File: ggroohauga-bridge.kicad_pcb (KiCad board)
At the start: 2 copper layers, 98.5 x 31 mm, 12 parts

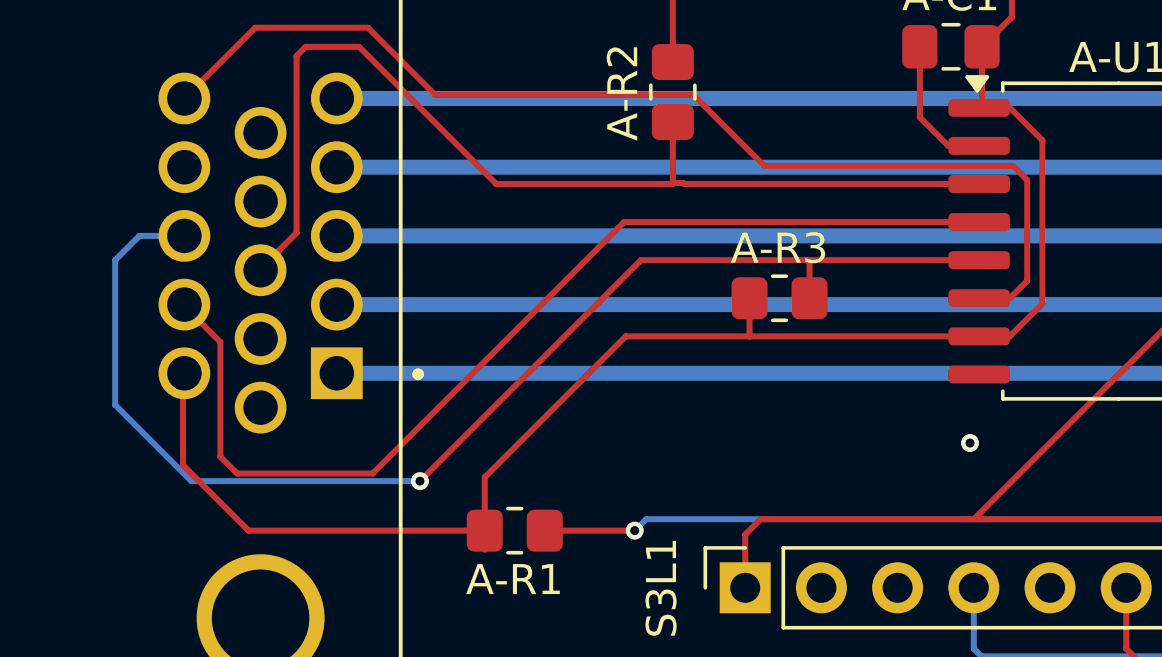
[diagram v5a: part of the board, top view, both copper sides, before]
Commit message: Move pull-up from AMP_RX to AMP_TX
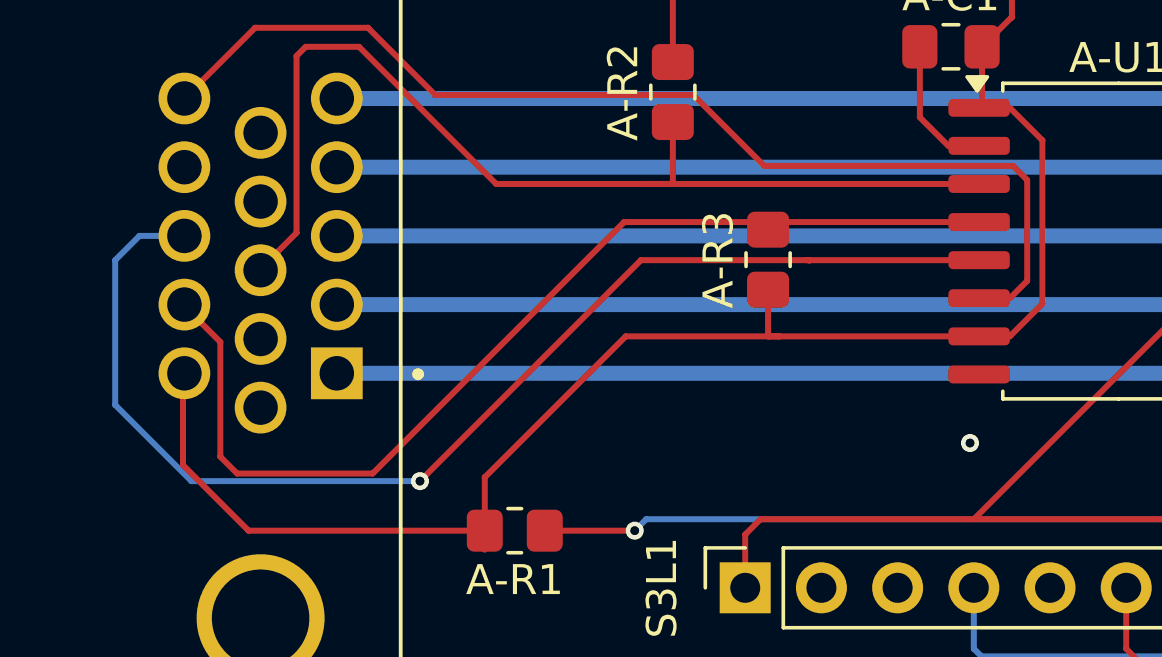
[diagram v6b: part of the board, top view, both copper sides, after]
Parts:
- moved A-R3 1.34 mm to (82.3, 66.5), turned to 90 degrees
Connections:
- A-R3 pad 2: /Common/AMP_RX -> /Common/AMP_TX
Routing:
- net /Common/AMP_RX: track 41.7 -> 40.5 mm
- net /Common/AMP_DETECT: track 34.5 -> 35.5 mm
- net /Common/AMP_TX: track 34.6 -> 33.8 mm
- net /Common/AMP_POWER_IN: track 74.8 -> 75.5 mm
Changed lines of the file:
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@@
 	(footprint "Resistor_SMD:R_0805_2012Metric_Pad1.20x1.40mm_HandSolder"
 		(layer "F.Cu")
-		(at 82.677 67.818)
+		(at 82.296 66.532 90)
 		(descr "Resistor SMD 0805 (2012 Metric), square (rectangular) end terminal, IPC-7351 nominal with elongated pad for handsoldering. (Body size source: IPC-SM-782 page 72, https://www.pcb-3d.com/wordpress/wp-content/uploads/ipc-sm-782a_amendment_1_and_2.pdf), generated with kicad-footprint-generator")
 		(tags "resistor handsolder")
 		(property "Reference" "A-R3"
-			(at 0 -1.65 0)
+			(at 0 -1.65 90)
 			(layer "F.SilkS")
 			(effects
@@
 		)
 		(property "Value" "10kΩ"
-			(at 0 1.65 0)
+			(at 0 1.65 90)
 			(layer "F.Fab")
 			(effects
@@
 		)
 		(property "Datasheet" ""
-			(at 0 0 0)
+			(at 0 0 90)
 			(layer "F.Fab")
 			(hide yes)
@@
 		)
 		(property "Description" "Resistor"
-			(at 0 0 0)
+			(at 0 0 90)
 			(layer "F.Fab")
 			(hide yes)
@@
 		)
 		(fp_line
-			(start -1.85 -0.95)
-			(end 1.85 -0.95)
+			(start 1.85 -0.95)
+			(end 1.85 0.95)
 			(stroke
 				(width 0.05)
@@
 		)
 		(fp_line
-			(start -1.85 0.95)
-			(end -1.85 -0.95)
+			(start -1.85 -0.95)
+			(end 1.85 -0.95)
 			(stroke
 				(width 0.05)
@@
 		)
 		(fp_line
-			(start 1.85 -0.95)
-			(end 1.85 0.95)
+			(start 1.85 0.95)
+			(end -1.85 0.95)
 			(stroke
 				(width 0.05)
@@
 		)
 		(fp_line
-			(start 1.85 0.95)
-			(end -1.85 0.95)
+			(start -1.85 0.95)
+			(end -1.85 -0.95)
 			(stroke
 				(width 0.05)
@@
 		)
 		(fp_line
-			(start -1 -0.625)
-			(end 1 -0.625)
+			(start 1 -0.625)
+			(end 1 0.625)
 			(stroke
 				(width 0.1)
@@
 		)
 		(fp_line
-			(start -1 0.625)
-			(end -1 -0.625)
+			(start -1 -0.625)
+			(end 1 -0.625)
 			(stroke
 				(width 0.1)
@@
 		)
 		(fp_line
-			(start 1 -0.625)
-			(end 1 0.625)
+			(start 1 0.625)
+			(end -1 0.625)
 			(stroke
 				(width 0.1)
@@
 		)
 		(fp_line
-			(start 1 0.625)
-			(end -1 0.625)
+			(start -1 0.625)
+			(end -1 -0.625)
 			(stroke
 				(width 0.1)
@@
 		)
 		(fp_text user "${REFERENCE}"
-			(at 0 0 0)
+			(at 0 0 90)
 			(layer "F.Fab")
 			(effects
@@
 		)
 		(pad "1" smd roundrect
-			(at -1 0)
+			(at -1 0 90)
 			(size 1.2 1.4)
 			(layers "F.Cu" "F.Mask" "F.Paste")
@@
 		)
 		(pad "2" smd roundrect
-			(at 1 0)
+			(at 1 0 90)
 			(size 1.2 1.4)
 			(layers "F.Cu" "F.Mask" "F.Paste")
 			(roundrect_rratio 0.208333)
-			(net 5 "/Common/AMP_RX")
+			(net 4 "/Common/AMP_TX")
 			(pintype "passive")
 		)
@@
 	)
 	(segment
-		(start 81.677 69.072)
-		(end 81.693 69.088)
+		(start 82.296 67.532)
+		(end 82.296 69.088)
 		(width 0.2)
 		(layer "F.Cu")
@@
 	)
 	(segment
-		(start 81.693 69.088)
+		(start 82.296 69.088)
+		(end 82.677 69.088)
+		(width 0.2)
+		(layer "F.Cu")
+		(net 3)
+	)
+	(segment
+		(start 72.8516 76.2)
+		(end 72.8516 73.787)
+		(width 0.2)
+		(layer "F.Cu")
+		(net 3)
+	)
+	(segment
+		(start 82.677 69.088)
 		(end 89.33 69.088)
 		(width 0.2)
@@
 	)
 	(segment
-		(start 89.4295 59.436)
-		(end 89.4295 61.3685)
+		(start 77.5506 69.088)
+		(end 82.677 69.088)
 		(width 0.2)
 		(layer "F.Cu")
@@
 	)
 	(segment
-		(start 81.677 67.818)
-		(end 81.677 69.072)
+		(start 89.4295 59.436)
+		(end 89.4295 61.3685)
 		(width 0.2)
 		(layer "F.Cu")
@@
 	)
 	(segment
-		(start 81.677 69.072)
-		(end 81.661 69.088)
-		(width 0.2)
-		(layer "F.Cu")
-		(net 3)
-	)
-	(segment
 		(start 72.8516 75.565)
 		(end 64.9776 75.565)
@@
 	)
 	(segment
-		(start 72.8516 76.2)
-		(end 72.8516 73.787)
-		(width 0.2)
-		(layer "F.Cu")
-		(net 3)
-	)
-	(segment
 		(start 90.424 53.34)
 		(end 90.424 58.4575)
@@
 	)
 	(segment
-		(start 72.8516 73.787)
-		(end 77.5506 69.088)
-		(width 0.2)
-		(layer "F.Cu")
-		(net 3)
-	)
-	(segment
 		(start 90.424 58.4575)
 		(end 90.408 58.4575)
@@
 	)
 	(segment
-		(start 77.5506 69.088)
-		(end 81.661 69.088)
+		(start 72.8516 73.787)
+		(end 77.5506 69.088)
 		(width 0.2)
 		(layer "F.Cu")
@@
 	)
 	(segment
-		(start 69.115618 73.66)
+		(start 82.042 65.278)
 		(end 77.497618 65.278)
 		(width 0.2)
@@
 	(segment
 		(start 64.0378 69.2742)
-		(end 64.0378 73.1012)
+		(end 62.7928 68.0292)
 		(width 0.2)
 		(layer "F.Cu")
@@
 	(segment
 		(start 64.0378 73.1012)
-		(end 64.5966 73.66)
+		(end 64.0378 69.2742)
 		(width 0.2)
 		(layer "F.Cu")
@@
 	)
 	(segment
-		(start 62.7928 68.0292)
-		(end 64.0378 69.2742)
+		(start 64.5966 73.66)
+		(end 64.0378 73.1012)
 		(width 0.2)
 		(layer "F.Cu")
@@
 	(segment
 		(start 77.497618 65.278)
+		(end 69.115618 73.66)
+		(width 0.2)
+		(layer "F.Cu")
+		(net 4)
+	)
+	(segment
+		(start 82.804 65.278)
 		(end 89.33 65.278)
 		(width 0.2)
@@
 	)
 	(segment
-		(start 64.5966 73.66)
-		(end 69.115618 73.66)
+		(start 69.115618 73.66)
+		(end 64.5966 73.66)
 		(width 0.2)
 		(layer "F.Cu")
@@
 	)
 	(segment
-		(start 83.677 67.818)
-		(end 83.677 66.564)
-		(width 0.2)
-		(layer "F.Cu")
-		(net 5)
-	)
-	(segment
 		(start 83.566 66.548)
 		(end 83.693 66.548)
@@
 	)
 	(segment
-		(start 79.47 63.976)
-		(end 79.502 64.008)
+		(start 78.105 64.008)
+		(end 73.2326 64.008)
 		(width 0.2)
 		(layer "F.Cu")
@@
 	)
 	(segment
-		(start 79.121 63.976)
-		(end 79.47 63.976)
+		(start 89.33 64.008)
+		(end 78.105 64.008)
 		(width 0.2)
 		(layer "F.Cu")
@@
 	(segment
 		(start 79.121 64.008)
-		(end 73.2326 64.008)
+		(end 78.105 64.008)
 		(width 0.2)
 		(layer "F.Cu")
@@
 		(width 0.2)
 		(layer "F.Cu")
-		(net 7)
-	)
-	(segment
-		(start 79.502 64.008)
-		(end 89.33 64.008)
-		(width 0.2)
-		(layer "F.Cu")

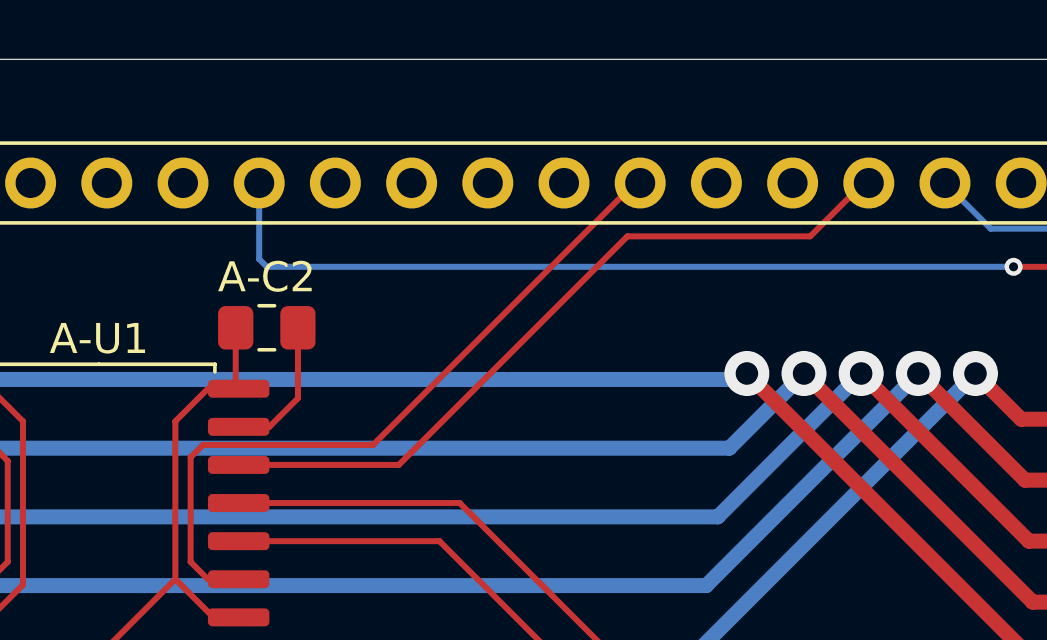
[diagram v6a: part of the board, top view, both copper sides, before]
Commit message: Fix GPIO assignments
Stop using GPIO 14 because the pull-up isn't working reliably on my LOLIN
S3 board even when floating and I don't have another one to test it with.

Don't use GPIO 35 on the DevKitC-1 board because that conflicts with the
Octal PSRAM.
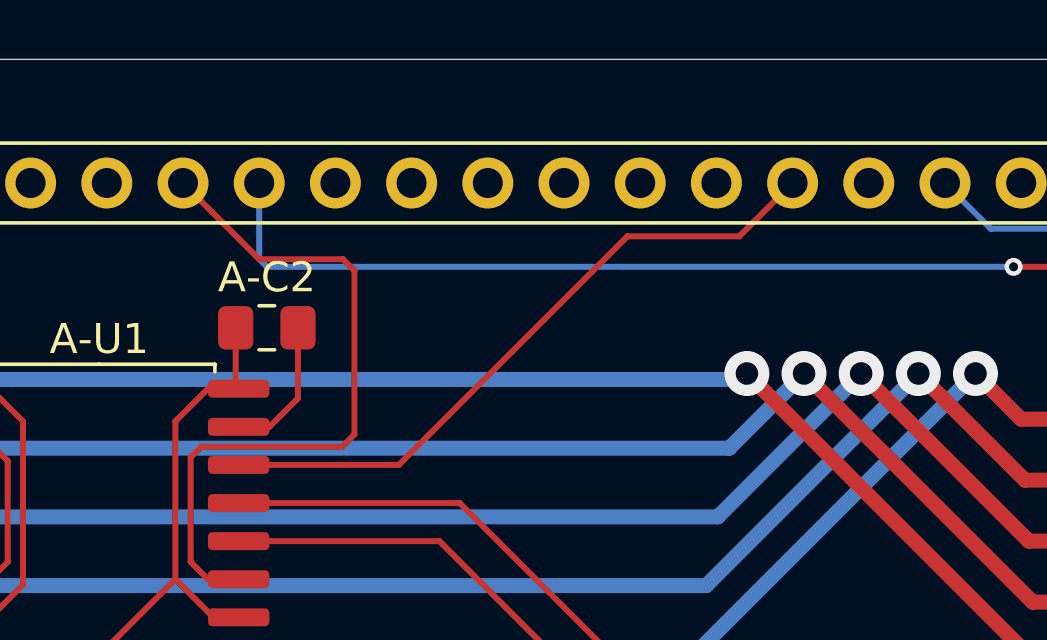
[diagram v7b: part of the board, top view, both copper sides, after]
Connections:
- A-U1 pad 11: /Common/GPIO_L48_C35_M36/CON_ANNOUNCE -> /Common/GPIO_L41_C41_M42/CON_ANNOUNCE
- A-U1 pad 14: /Common/GPIO_L14_C48_M33/AMP_DETECT -> /Common/GPIO_L21_C21_M21/AMP_DETECT
- S3R1 pad 13: /Common/GPIO_L48_C35_M36/CON_ANNOUNCE -> unconnected-(S3R1-Pin_13-Pad13)
- S3R1 pad 14: GND -> unconnected-(S3R1-Pin_14-Pad14)
- S3R1 pad 15: GND -> /Common/GPIO_L21_C21_M21/AMP_DETECT
- S3R1 pad 16: /Common/GPIO_L14_C48_M33/AMP_DETECT -> GND
- S3R1 pad 7: GND -> /Common/GPIO_L41_C41_M42/CON_ANNOUNCE
- S3R1 pad 9: GND -> unconnected-(S3R1-Pin_9-Pad9)
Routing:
- net /Common/GPIO_L14_C48_M33/AMP_DETECT: track 24.7 -> 0.00 mm
- net /Common/GPIO_L48_C35_M36/CON_ANNOUNCE: track 23.9 -> 0.00 mm
- net /Common/GPIO_L41_C41_M42/CON_ANNOUNCE: track 0.00 -> 23.5 mm
- net /Common/GPIO_L21_C21_M21/AMP_DETECT: track 0.00 -> 22.4 mm
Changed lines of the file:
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@@
 	(net 16 "/Common/GPIO_L9_C9_M13{slash}AMP_TX")
 	(net 17 "/Common/GPIO_L10_C10_M14{slash}AMP_RX")
-	(net 18 "/Common/GPIO_L48_C35_M36{slash}CON_ANNOUNCE")
-	(net 19 "/Common/GPIO_L14_C48_M33{slash}AMP_DETECT")
+	(net 18 "/Common/GPIO_L41_C41_M42{slash}CON_ANNOUNCE")
+	(net 19 "/Common/GPIO_L21_C21_M21{slash}AMP_DETECT")
 	(net 20 "+3.3V")
 	(net 21 "/Common/GPIO_L17_C17_M8{slash}CON_DETECT")
@@
 	(net 48 "unconnected-(C-J1-Pad7)")
 	(net 49 "unconnected-(S3L1-Pin_2-Pad2)")
+	(net 50 "unconnected-(S3R1-Pin_14-Pad14)")
+	(net 51 "unconnected-(S3R1-Pin_9-Pad9)")
+	(net 52 "unconnected-(S3R1-Pin_13-Pad13)")
 	(footprint "Resistor_SMD:R_0805_2012Metric_Pad1.20x1.40mm_HandSolder"
 		(layer "F.Cu")
@@
 			(layers "*.Cu" "*.Mask")
 			(remove_unused_layers no)
-			(net 36 "GND")
+			(net 18 "/Common/GPIO_L41_C41_M42{slash}CON_ANNOUNCE")
 			(pinfunction "Pin_7")
 			(pintype "passive")
@@
 			(layers "*.Cu" "*.Mask")
 			(remove_unused_layers no)
-			(net 36 "GND")
+			(net 51 "unconnected-(S3R1-Pin_9-Pad9)")
 			(pinfunction "Pin_9")
-			(pintype "passive")
+			(pintype "passive+no_connect")
 		)
 		(pad "10" thru_hole circle
@@
 			(layers "*.Cu" "*.Mask")
 			(remove_unused_layers no)
-			(net 18 "/Common/GPIO_L48_C35_M36{slash}CON_ANNOUNCE")
+			(net 52 "unconnected-(S3R1-Pin_13-Pad13)")
 			(pinfunction "Pin_13")
-			(pintype "passive")
+			(pintype "passive+no_connect")
 		)
 		(pad "14" thru_hole circle
@@
 			(layers "*.Cu" "*.Mask")
 			(remove_unused_layers no)
-			(net 36 "GND")
+			(net 50 "unconnected-(S3R1-Pin_14-Pad14)")
 			(pinfunction "Pin_14")
-			(pintype "passive")
+			(pintype "passive+no_connect")
 		)
 		(pad "15" thru_hole circle
@@
 			(layers "*.Cu" "*.Mask")
 			(remove_unused_layers no)
-			(net 36 "GND")
+			(net 19 "/Common/GPIO_L21_C21_M21{slash}AMP_DETECT")
 			(pinfunction "Pin_15")
 			(pintype "passive")
@@
 			(layers "*.Cu" "*.Mask")
 			(remove_unused_layers no)
-			(net 19 "/Common/GPIO_L14_C48_M33{slash}AMP_DETECT")
+			(net 36 "GND")
 			(pinfunction "Pin_16")
 			(pintype "passive")
@@
 			(layers "F.Cu" "F.Mask" "F.Paste")
 			(roundrect_rratio 0.25)
-			(net 18 "/Common/GPIO_L48_C35_M36{slash}CON_ANNOUNCE")
+			(net 18 "/Common/GPIO_L41_C41_M42{slash}CON_ANNOUNCE")
 			(pinfunction "IND")
 			(pintype "input")
@@
 			(layers "F.Cu" "F.Mask" "F.Paste")
 			(roundrect_rratio 0.25)
-			(net 19 "/Common/GPIO_L14_C48_M33{slash}AMP_DETECT")
+			(net 19 "/Common/GPIO_L21_C21_M21{slash}AMP_DETECT")
 			(pinfunction "OUTA")
 			(pintype "output")
@@
 	)
 	(segment
-		(start 97.028 63.754)
-		(end 97.028 67.240999)
+		(start 96.774 54.61)
+		(end 99.314 57.15)
 		(width 0.2)
 		(layer "F.Cu")
@@
 	)
 	(segment
-		(start 97.605001 67.818)
-		(end 98.63 67.818)
+		(start 97.3836 63.3984)
+		(end 97.028 63.754)
 		(width 0.2)
 		(layer "F.Cu")
@@
 	)
 	(segment
-		(start 97.443 63.339)
-		(end 97.028 63.754)
+		(start 102.0826 63.3984)
+		(end 97.3836 63.3984)
+		(width 0.2)
+		(layer "F.Cu")
+		(net 18)
+	)
+	(segment
+		(start 102.489 62.992)
+		(end 102.0826 63.3984)
 		(width 0.2)
 		(layer "F.Cu")
@@
 	)
 	(segment
-		(start 111.8406 54.61)
-		(end 103.1116 63.339)
+		(start 99.314 57.15)
+		(end 102.108 57.15)
 		(width 0.2)
 		(layer "F.Cu")
@@
 	)
 	(segment
-		(start 103.1116 63.339)
-		(end 97.443 63.339)
+		(start 102.489 57.531)
+		(end 102.489 62.992)
+		(width 0.2)
+		(layer "F.Cu")
+		(net 18)
+	)
+	(segment
+		(start 97.605001 67.818)
+		(end 98.63 67.818)
+		(width 0.2)
+		(layer "F.Cu")
+		(net 18)
+	)
+	(segment
+		(start 97.028 63.754)
+		(end 97.028 67.240999)
 		(width 0.2)
 		(layer "F.Cu")
@@
 	)
 	(segment
-		(start 117.6826 56.388)
-		(end 119.4606 54.61)
+		(start 102.108 57.15)
+		(end 102.489 57.531)
 		(width 0.2)
 		(layer "F.Cu")
-		(net 19)
+		(net 18)
 	)
 	(segment
@@
 	)
 	(segment
-		(start 111.5866 56.388)
-		(end 117.6826 56.388)
+		(start 103.9666 64.008)
+		(end 111.5866 56.388)
 		(width 0.2)
 		(layer "F.Cu")
@@
 	)
 	(segment
-		(start 103.9666 64.008)
-		(end 111.5866 56.388)
+		(start 115.316 56.388)
+		(end 117.094 54.61)
+		(width 0.2)
+		(layer "F.Cu")
+		(net 19)
+	)
+	(segment
+		(start 111.5866 56.388)
+		(end 115.316 56.388)
 		(width 0.2)
 		(layer "F.Cu")
